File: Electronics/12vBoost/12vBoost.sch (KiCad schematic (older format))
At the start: 19 parts

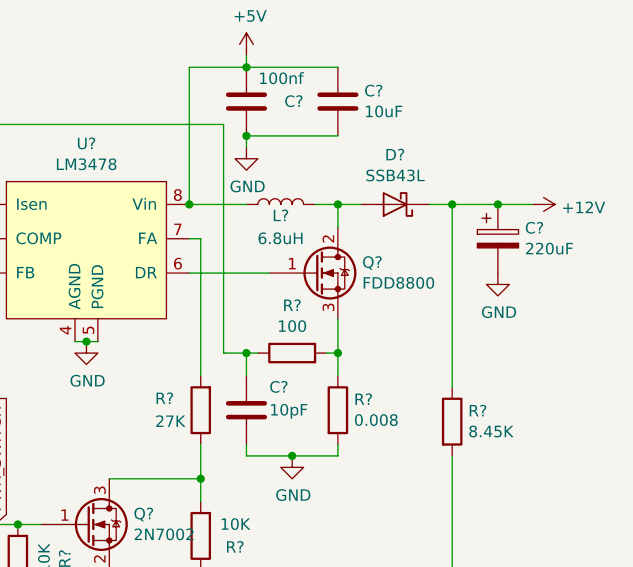
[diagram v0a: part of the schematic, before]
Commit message: fix 12vboost transistor typo
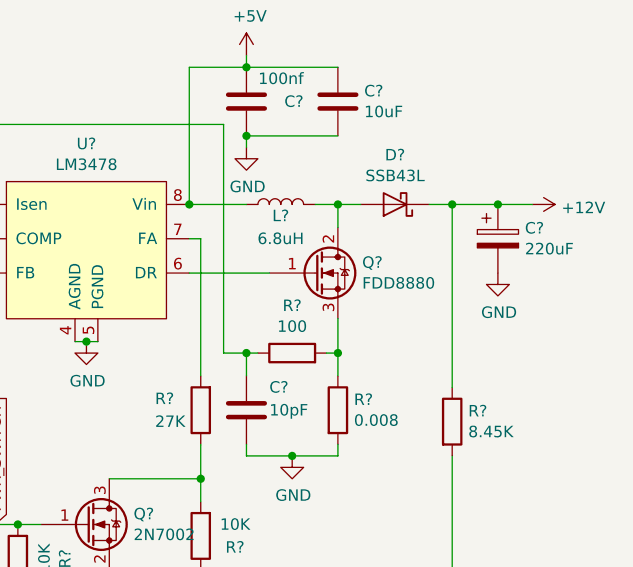
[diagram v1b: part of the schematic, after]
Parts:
- Q?: value FDD8800 -> FDD8880
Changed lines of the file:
@@
 P 6200 3200
 F 0 "Q?" H 6406 3246 50  0000 L CNN
-F 1 "FDD8800" H 6406 3155 50  0000 L CNN
+F 1 "FDD8880" H 6406 3155 50  0000 L CNN
 F 2 "Package_TO_SOT_SMD:TO-252-2" H 6400 3300 50  0001 C CNN
 F 3 "~" H 6200 3200 50  0001 C CNN

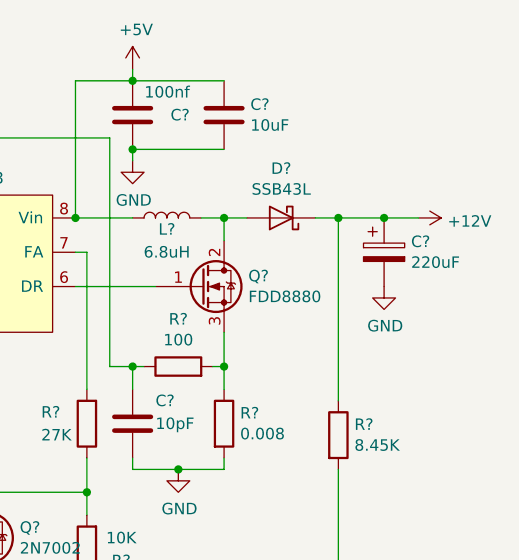
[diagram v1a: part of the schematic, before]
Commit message: 3v3 boost in dip body
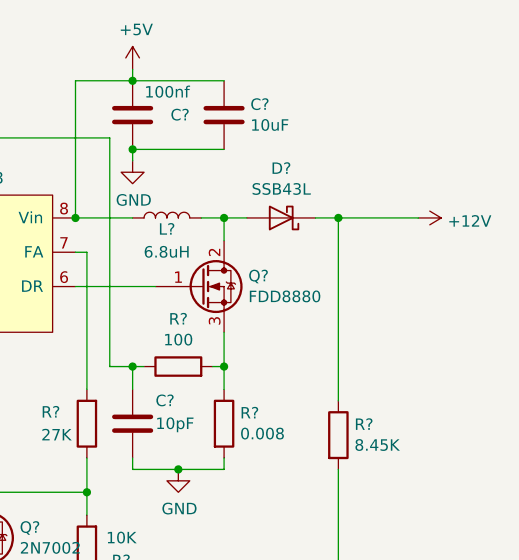
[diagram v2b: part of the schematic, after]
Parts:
- removed C?: 220uF, Capacitor_SMD:CP_Elec_8x10.5, symbol EggbotWireless-rescue:CP-Device
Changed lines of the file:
@@
 Connection ~ 5900 3550
-$Comp
-L EggbotWireless-rescue:CP-Device C?
-U 1 1 5FE802A1
-P 7000 3050
-F 0 "C?" H 7118 3096 50  0000 L CNN
-F 1 "220uF" H 7118 3005 50  0000 L CNN
-F 2 "Capacitor_SMD:CP_Elec_8x10.5" H 7038 2900 50  0001 C CNN
-F 3 "~" H 7000 3050 50  0001 C CNN
-	1    7000 3050
-	1    0    0    -1
-$EndComp
-$Comp
-L EggbotWireless-rescue:GND-power-Catfi-rescue #PWR?
-U 1 1 5FE802A7
-P 7000 3200
-F 0 "#PWR?" H 7000 2950 50  0001 C CNN
-F 1 "GND" H 7005 3027 50  0000 C CNN
-F 2 "" H 7000 3200 50  0001 C CNN
-F 3 "" H 7000 3200 50  0001 C CNN
-	1    7000 3200
-	1    0    0    -1
-$EndComp
 $Comp
 L EggbotWireless-rescue:GND-power-Catfi-rescue #PWR?
@@
 	6800 2900 6800 3700
 Connection ~ 6800 2900
-Wire Wire Line
-	6800 2900 7000 2900
 Wire Wire Line
 	6800 4000 6800 4750
@@
 	4900 4650 5300 4650
 Connection ~ 5300 4650
-Connection ~ 7000 2900
-Wire Wire Line
-	7000 2900 7150 2900
 $Comp
 L EggbotWireless-rescue:+12V-power #PWR?
@@
 	1    0    0    -1
 $EndComp
+Wire Wire Line
+	6800 2900 7150 2900
 $EndSCHEMATC

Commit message: 12vBoost module
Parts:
- added U2: 12vBoost, 12vBoost:12vBoost, symbol 12vBoost:12vBoost
- C1, C2, C3, C4, C5: renamed from C?; footprint Capacitor_SMD:C_0805_2012Metric_Pad1.15x1.40mm_HandSolder -> Capacitor_SMD:C_0805_2012Metric_Pad1.18x1.45mm_HandSolder
- R1, R2, R3, R4, R5, R6, R8: renamed from R?; footprint Resistor_SMD:R_0805_2012Metric_Pad1.15x1.40mm_HandSolder -> Resistor_SMD:R_0805_2012Metric_Pad1.20x1.40mm_HandSolder
- R7: renamed from R?; footprint Resistor_SMD:R_1206_3216Metric_Pad1.42x1.75mm_HandSolder -> Resistor_SMD:R_1206_3216Metric_Pad1.30x1.75mm_HandSolder
- gave numbers to parts that had none: 5
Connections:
- net +12V: now also U2.5 (12V), U2.6 (12V)
- net +3V3: now also U2.15 (3V3)
- net +5V: now also U2.1 (5V), U2.2 (5V)
- net GND: now also U2.3 (GND), U2.4 (GND)
- net PWR_SWITCH: now also U2.9 (ON)
